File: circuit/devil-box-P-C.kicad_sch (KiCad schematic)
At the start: 18 parts, among them M1 Motor_Servo, T1 BSS123, T2 BSS123, T3 BSS123, T4 IRF9540N, T5 BSS123

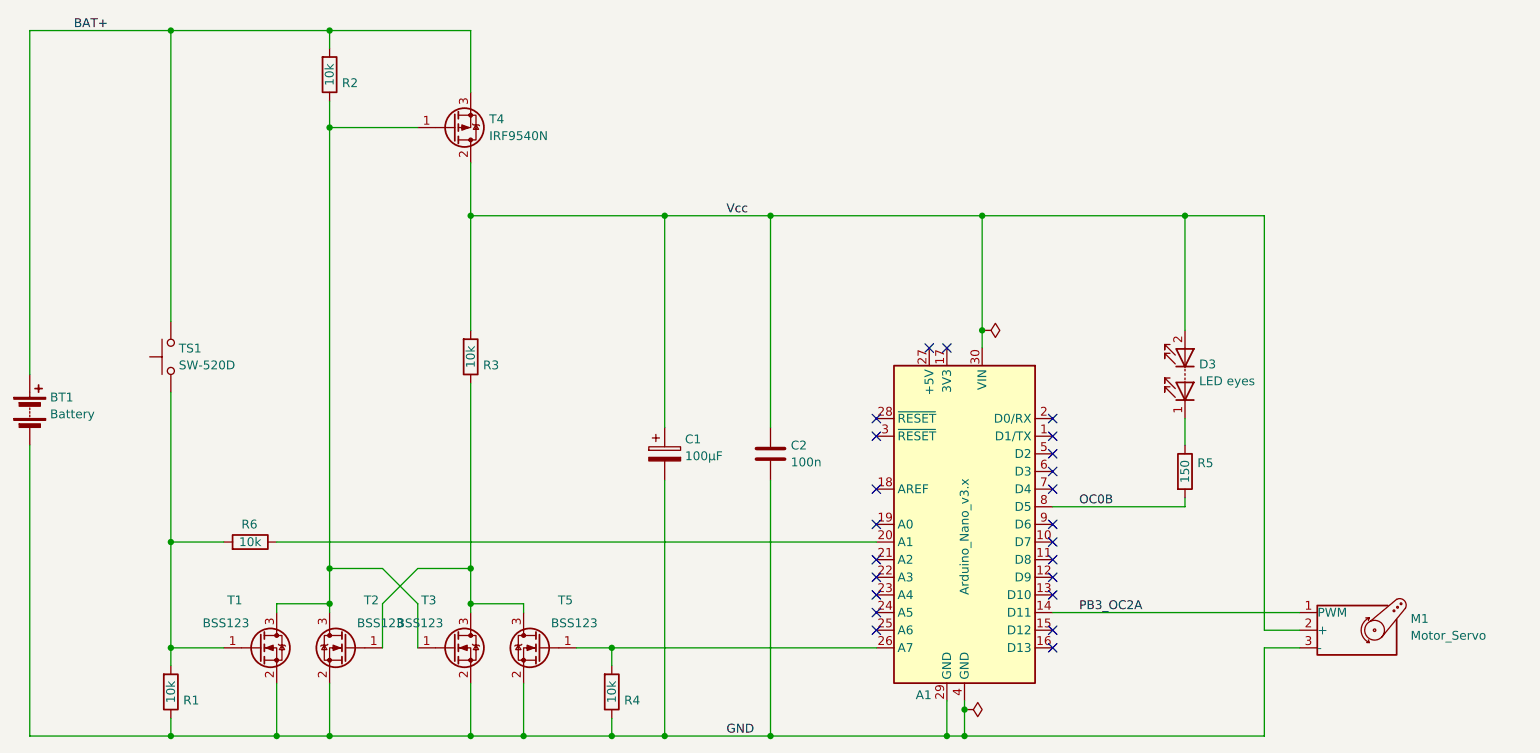
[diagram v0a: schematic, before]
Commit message: change P-MOSFET to IRF9Z34N, add color labels to servo wires
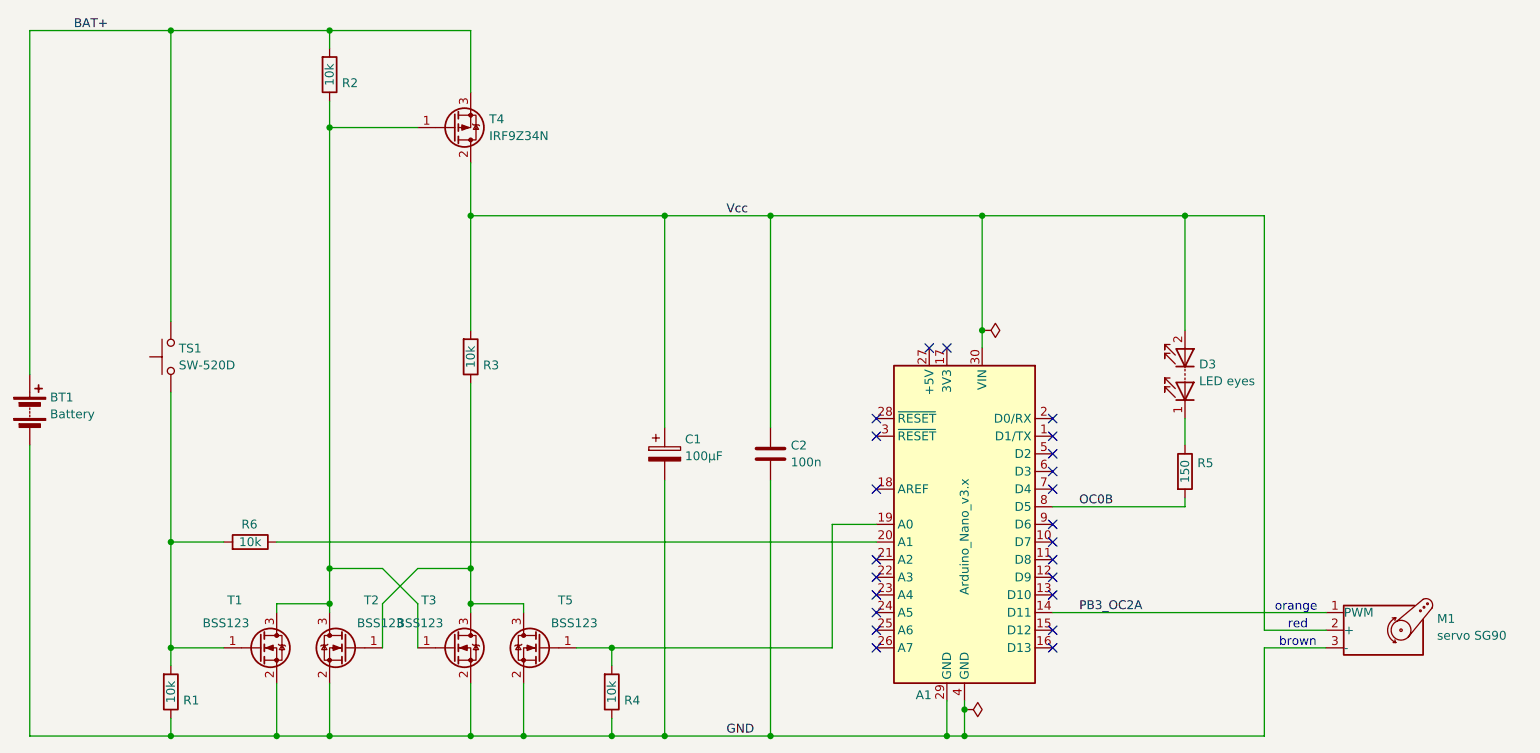
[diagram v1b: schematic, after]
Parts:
- M1: value Motor_Servo -> servo SG90
- T4: value IRF9540N -> IRF9Z34N
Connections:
- net at R4.2, T5.1 (G): now also A1.19 (A0); no longer A1.26 (A7)
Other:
- note added: "brown"
- note added: "orange"
- note added: "red"
- moved on the sheet: M1
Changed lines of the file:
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@@
 	)
 	(no_connect
-		(at 167.64 111.76)
+		(at 167.64 129.54)
 	)
 	(no_connect
@@
 	(wire
 		(pts
+			(xy 167.64 111.76) (xy 161.29 111.76)
+		)
+		(stroke
+			(width 0)
+			(type default)
+		)
+	)
+	(wire
+		(pts
 			(xy 129.54 139.7) (xy 129.54 142.24)
 		)
@@
 	(wire
 		(pts
-			(xy 129.54 129.54) (xy 167.64 129.54)
+			(xy 129.54 129.54) (xy 161.29 129.54)
 		)
 		(stroke
@@
 	(wire
 		(pts
-			(xy 223.52 129.54) (xy 228.6 129.54)
+			(xy 223.52 129.54) (xy 232.41 129.54)
 		)
 		(stroke
@@
 	(wire
 		(pts
-			(xy 223.52 127) (xy 228.6 127)
-		)
-		(stroke
-			(width 0)
-			(type default)
-		)
-	)
-	(wire
-		(pts
-			(xy 193.04 124.46) (xy 228.6 124.46)
+			(xy 223.52 127) (xy 232.41 127)
+		)
+		(stroke
+			(width 0)
+			(type default)
+		)
+	)
+	(wire
+		(pts
+			(xy 193.04 124.46) (xy 232.41 124.46)
 		)
 		(stroke
@@
 	(wire
 		(pts
+			(xy 161.29 111.76) (xy 161.29 129.54)
+		)
+		(stroke
+			(width 0)
+			(type default)
+		)
+	)
+	(wire
+		(pts
 			(xy 180.34 137.16) (xy 180.34 138.43)
 		)
@@
 			(width 0)
 			(type default)
+		)
+	)
+	(text "red\n"
+		(exclude_from_sim no)
+		(at 228.346 126.238 0)
+		(effects
+			(font
+				(size 1.27 1.27)
+			)
+		)
+	)
+	(text "orange"
+		(exclude_from_sim no)
+		(at 228.092 123.698 0)
+		(effects
+			(font
+				(size 1.27 1.27)
+			)
+		)
+	)
+	(text "brown\n"
+		(exclude_from_sim no)
+		(at 228.346 128.778 0)
+		(effects
+			(font
+				(size 1.27 1.27)
+			)
 		)
 	)
@@
 		(fields_autoplaced yes)
 		(property "Reference" "T4"
-			(at 111.887 53.3979 0)
-			(effects
-				(font
-					(size 1.27 1.27)
-				)
-				(justify left)
-			)
-		)
-		(property "Value" "IRF9540N"
+			(at 111.887 53.3978 0)
+			(effects
+				(font
+					(size 1.27 1.27)
+				)
+				(justify left)
+			)
+		)
+		(property "Value" "IRF9Z34N"
 			(at 111.887 55.8221 0)
 			(effects
@@
 	(symbol
 		(lib_id "Motor:Motor_Servo")
-		(at 236.22 127 0)
+		(at 240.03 127 0)
 		(unit 1)
 		(exclude_from_sim no)
@@
 		(fields_autoplaced yes)
 		(property "Reference" "M1"
-			(at 244.5798 125.3545 0)
-			(effects
-				(font
-					(size 1.27 1.27)
-				)
-				(justify left)
-			)
-		)
-		(property "Value" "Motor_Servo"
-			(at 244.5798 127.7787 0)
+			(at 248.3898 125.3544 0)
+			(effects
+				(font
+					(size 1.27 1.27)
+				)
+				(justify left)
+			)
+		)
+		(property "Value" "servo SG90"
+			(at 248.3898 127.7787 0)
 			(effects
 				(font
@@
 		)
 		(property "Footprint" "Connector_PinHeader_2.54mm:PinHeader_1x03_P2.54mm_Vertical"
-			(at 236.22 131.826 0)
+			(at 240.03 131.826 0)
 			(effects
 				(font
@@
 		)
 		(property "Datasheet" "http://forums.parallax.com/uploads/attachments/46831/74481.png"
-			(at 236.22 131.826 0)
+			(at 240.03 131.826 0)
 			(effects
 				(font
@@
 		)
 		(property "Description" ""
-			(at 236.22 127 0)
-			(effects
-				(font
+			(at 240.03 127 0)
+			(effects
+				(font

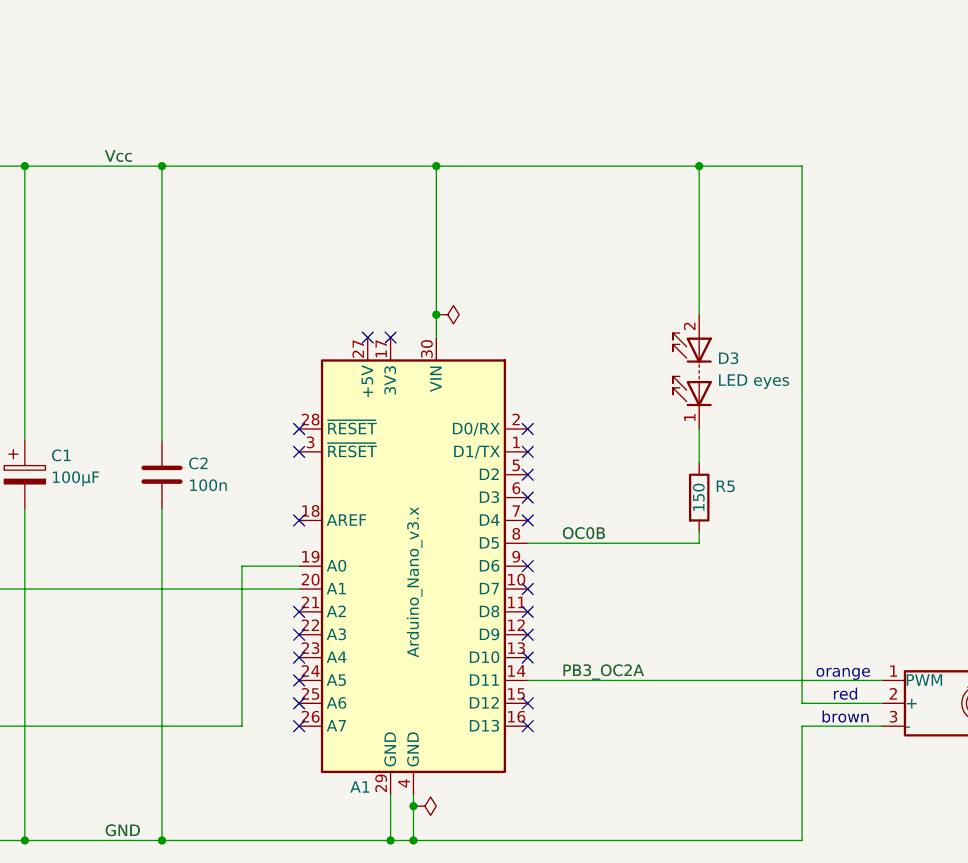
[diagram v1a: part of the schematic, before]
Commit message: add C3, D1
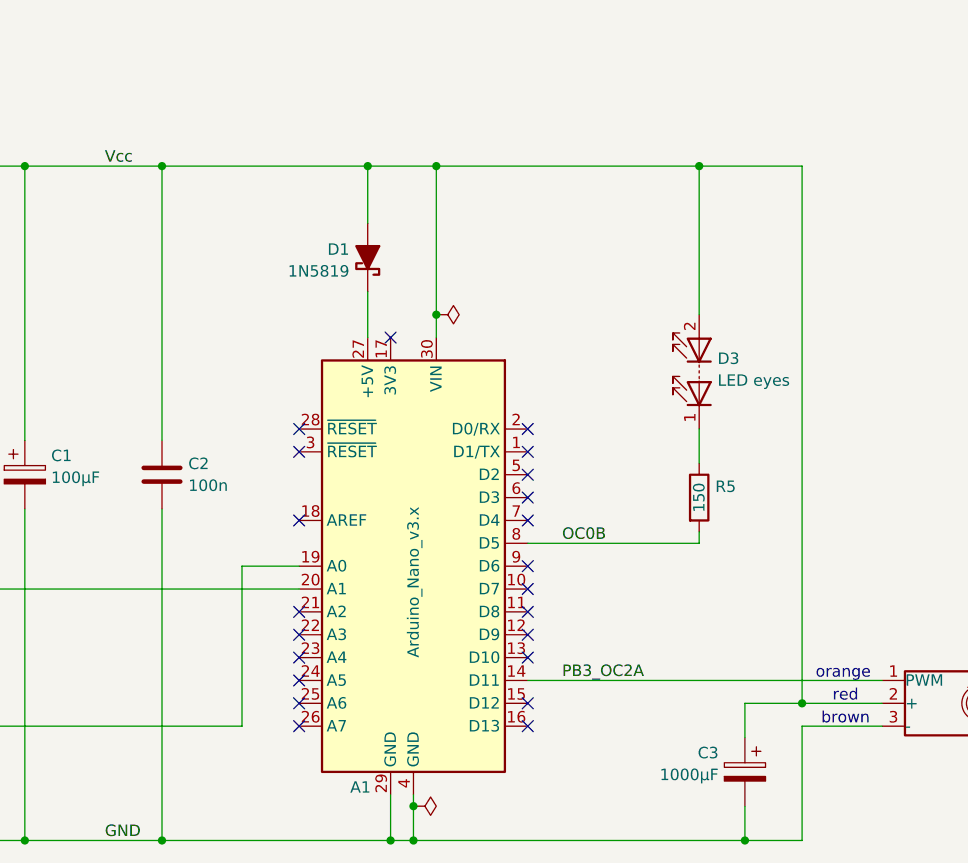
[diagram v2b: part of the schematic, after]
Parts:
- added C3: 1000μF, Capacitor_THT:CP_Radial_D5.0mm_P2.50mm, symbol Device:C_Polarized
- added D1: 1N5819, symbol Device:D_Schottky_Filled
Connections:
- net GND: now also C3.2
- net Vcc: now also C3.1, D1.2 (A)
- net at A1.27 (+5V): now also D1.1 (K)
- no-connect marks 23 -> 22
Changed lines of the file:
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@@
+	)
+	(junction
+		(at 217.17 142.24)
+		(diameter 0)
+		(color 0 0 0 0)
 	)
 	(junction
@@
 	)
 	(junction
+		(at 175.26 67.31)
+		(diameter 0)
+		(color 0 0 0 0)
+	)
+	(junction
 		(at 88.9 142.24)
 		(diameter 0)
@@
 	)
 	(junction
+		(at 223.52 127)
+		(diameter 0)
+		(color 0 0 0 0)
+	)
+	(junction
 		(at 66.04 142.24)
 		(diameter 0)
@@
 	)
 	(no_connect
-		(at 175.26 86.36)
-	)
-	(no_connect
 		(at 167.64 116.84)
 	)
@@
 	(wire
 		(pts
-			(xy 152.4 67.31) (xy 182.88 67.31)
+			(xy 152.4 67.31) (xy 175.26 67.31)
 		)
 		(stroke
@@
 	(wire
 		(pts
+			(xy 217.17 127) (xy 223.52 127)
+		)
+		(stroke
+			(width 0)
+			(type default)
+		)
+	)
+	(wire
+		(pts
 			(xy 180.34 138.43) (xy 180.34 142.24)
 		)
@@
 	(wire
 		(pts
+			(xy 175.26 67.31) (xy 175.26 73.66)
+		)
+		(stroke
+			(width 0)
+			(type default)
+		)
+	)
+	(wire
+		(pts
 			(xy 66.04 142.24) (xy 45.72 142.24)
 		)
@@
 	(wire
 		(pts
+			(xy 175.26 81.28) (xy 175.26 86.36)
+		)
+		(stroke
+			(width 0)
+			(type default)
+		)
+	)
+	(wire
+		(pts
 			(xy 96.52 123.19) (xy 96.52 129.54)
 		)
@@
 	(wire
 		(pts
+			(xy 217.17 142.24) (xy 223.52 142.24)
+		)
+		(stroke
+			(width 0)
+			(type default)
+		)
+	)
+	(wire
+		(pts
 			(xy 180.34 137.16) (xy 180.34 138.43)
 		)
@@
 	(wire
 		(pts
+			(xy 217.17 130.81) (xy 217.17 127)
+		)
+		(stroke
+			(width 0)
+			(type default)
+		)
+	)
+	(wire
+		(pts
 			(xy 66.04 132.08) (xy 66.04 129.54)
 		)
@@
 	(wire
 		(pts
+			(xy 175.26 67.31) (xy 182.88 67.31)
+		)
+		(stroke
+			(width 0)
+			(type default)
+		)
+	)
+	(wire
+		(pts
 			(xy 109.22 124.46) (xy 109.22 123.19)
 		)
@@
 	(wire
 		(pts
+			(xy 217.17 138.43) (xy 217.17 142.24)
+		)
+		(stroke
+			(width 0)
+			(type default)
+		)
+	)
+	(wire
+		(pts
 			(xy 116.84 142.24) (xy 116.84 134.62)
 		)
@@
 	(wire
 		(pts
-			(xy 180.34 142.24) (xy 223.52 142.24)
+			(xy 180.34 142.24) (xy 217.17 142.24)
 		)
 		(stroke
@@
 	)
 	(symbol
+		(lib_id "Device:D_Schottky_Filled")
+		(at 175.26 77.47 270)
+		(mirror x)
+		(unit 1)
+		(exclude_from_sim no)
+		(in_bom yes)
+		(on_board yes)
+		(dnp no)
+		(property "Reference" "D1"
+			(at 173.228 76.5753 90)
+			(effects
+				(font
+					(size 1.27 1.27)
+				)
+				(justify right)
+			)
+		)
+		(property "Value" "1N5819"
+			(at 173.228 78.9996 90)
+			(effects
+				(font
+					(size 1.27 1.27)
+				)
+				(justify right)
+			)
+		)
+		(property "Footprint" ""
+			(at 175.26 77.47 0)
+			(effects
+				(font
+					(size 1.27 1.27)
+				)
+				(hide yes)
+			)
+		)
+		(property "Datasheet" "~"
+			(at 175.26 77.47 0)
+			(effects
+				(font
+					(size 1.27 1.27)
+				)
+				(hide yes)
+			)
+		)
+		(property "Description" "Schottky diode, filled shape"
+			(at 175.26 77.47 0)
+			(effects
+				(font
+					(size 1.27 1.27)
+				)
+				(hide yes)
+			)
+		)
+		(pin "1"
+		)
+		(pin "2"
+		)
+		(instances
+			(project ""
+				(path "/c6112e97-0a50-4811-b9a7-b9d8fe3a9480"
+					(reference "D1")
+					(unit 1)
+				)
+			)
+		)
+	)
+	(symbol
 		(lib_id "Device:R")
 		(at 88.9 46.99 0)
@@
 					(unit 1)
 				)
+			)
+		)
+	)
+	(symbol
+		(lib_id "Device:C_Polarized")
+		(at 217.17 134.62 0)
+		(mirror y)
+		(unit 1)
+		(exclude_from_sim no)
+		(in_bom no)
+		(on_board yes)
+		(dnp no)
+		(property "Reference" "C3"
+			(at 214.249 132.5189 0)
+			(effects
+				(font
+					(size 1.27 1.27)
+				)
+				(justify left)
+			)
+		)
+		(property "Value" "1000μF"
+			(at 214.249 134.9431 0)
+			(effects
+				(font
+					(size 1.27 1.27)
+				)
+				(justify left)
+			)
+		)
+		(property "Footprint" "Capacitor_THT:CP_Radial_D5.0mm_P2.50mm"
+			(at 216.2048 138.43 0)
+			(effects
+				(font
+					(size 1.27 1.27)
+				)
+				(hide yes)
+			)
+		)
+		(property "Datasheet" "~"
+			(at 217.17 134.62 0)
+			(effects
+				(font
+					(size 1.27 1.27)
+				)
+				(hide yes)
+			)
+		)
+		(property "Description" ""
+			(at 217.17 134.62 0)
+			(effects
+				(font
+					(size 1.27 1.27)
+				)
+				(hide yes)
+			)
+		)
+		(pin "2"
+		)
+		(pin "1"
+		)
+		(instances
+			(project "devil-box-P-C"
+				(path "/c6112e97-0a50-4811-b9a7-b9d8fe3a9480"
+					(reference "C3")
+					(unit 1)
+				)
